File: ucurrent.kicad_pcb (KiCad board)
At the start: 2 copper layers, 44 x 64 mm, 40 parts, among them J1 Conn_01x02, J2 IN_P, J3 IN_N, J4 POWER, J5 Select, J6 OUT_P, J7 OUT_N, SW1 BAT_TEST, SW2 BAT_TEST, U1 TPS3839DBZ, U2 LMV321, U3 MAX4239AUT, U4 MAX4239AUT

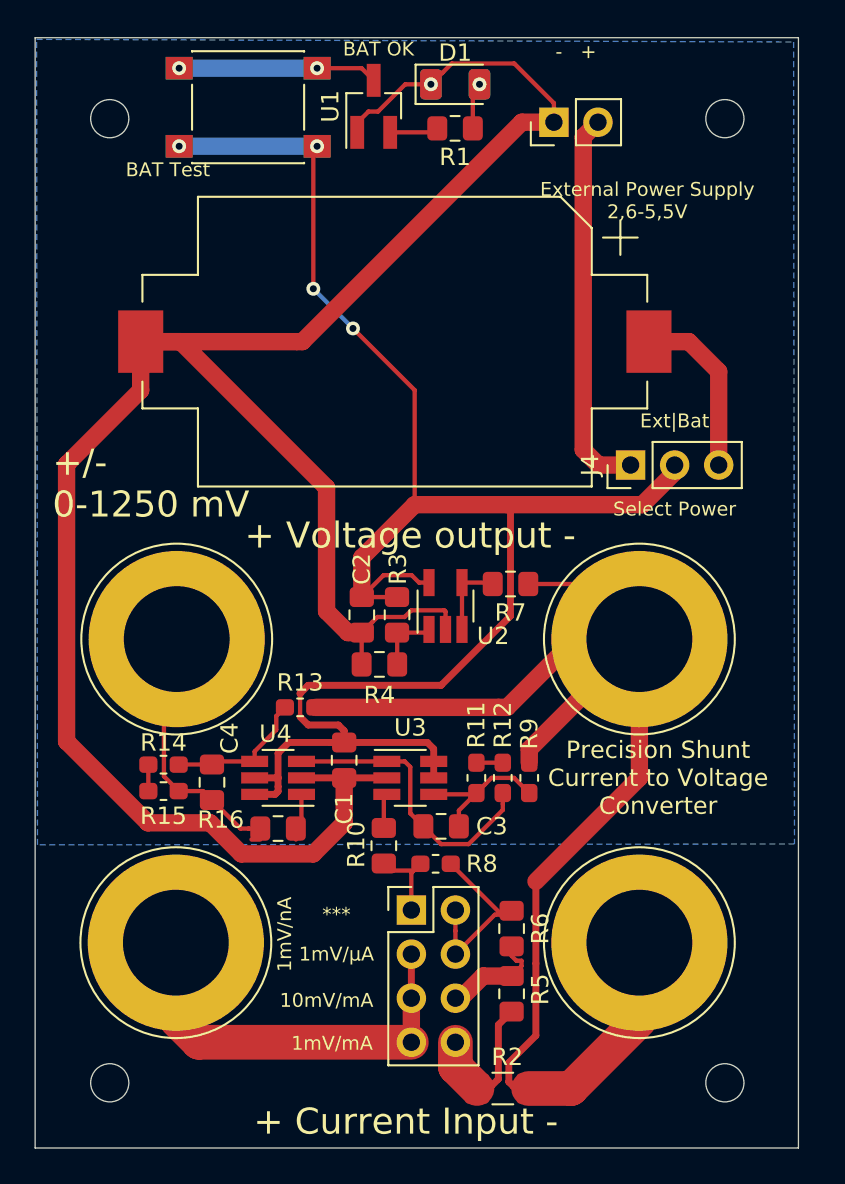
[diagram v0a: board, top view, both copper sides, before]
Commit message: Redid the schematic for voltage measurement, added JLCPCB component references.
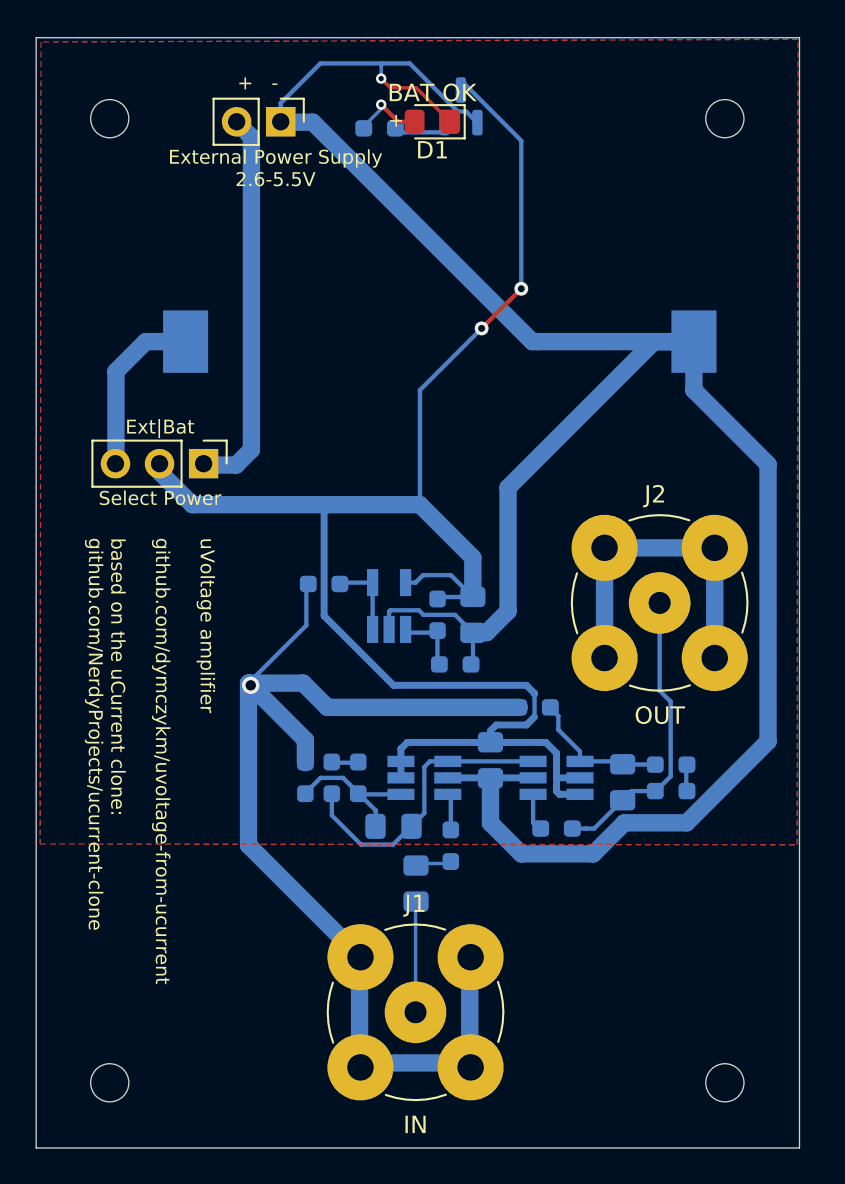
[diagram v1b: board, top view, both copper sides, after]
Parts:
- removed D2: GREEN, LED_SMD:LED_1206_3216Metric
- removed the J3 at (116.3, 93.1)
- removed J5: Select, Connector_PinHeader_2.54mm:PinHeader_2x04_P2.54mm_Vertical
- removed J6: OUT_P, Connector:Banana_Jack_1Pin
- removed J7: OUT_N, Connector:Banana_Jack_1Pin
- removed the R2 at (108.5, 101.5)
- removed the R5 at (109.0, 96.0)
- removed the R6 at (109.0, 92.3)
- removed the R8 at (104.6, 88.5)
- removed SW1, SW2: BAT_TEST, Button_Switch_SMD:SW_Push_1P1T_NO_6x6mm_H9.5mm
- added C1: 100n, Capacitor_SMD:C_0805_2012Metric_Pad1.18x1.45mm_HandSolder, B.Cu at (103.5, 89.7)
- added J1: IN, Connector_Coaxial:BNC_TEConnectivity_1478204_Vertical, F.Cu at (103.4, 97.1)
- BT1, H1, H2, H3, H4, U2, U3, U4: moved to B.Cu
- C2: renamed from C1; footprint Capacitor_SMD:C_0805_2012Metric_Pad1.15x1.40mm_HandSolder -> Capacitor_SMD:C_0805_2012Metric_Pad1.18x1.45mm_HandSolder; moved to B.Cu
- C3: renamed from C2; footprint Capacitor_SMD:C_0805_2012Metric_Pad1.15x1.40mm_HandSolder -> Capacitor_SMD:C_0805_2012Metric_Pad1.18x1.45mm_HandSolder; moved to B.Cu
- C4: renamed from C3; footprint Capacitor_SMD:C_0805_2012Metric_Pad1.15x1.40mm_HandSolder -> Capacitor_SMD:C_0805_2012Metric_Pad1.18x1.45mm_HandSolder; moved to B.Cu
- C5: renamed from C4; footprint Capacitor_SMD:C_0805_2012Metric_Pad1.15x1.40mm_HandSolder -> Capacitor_SMD:C_0805_2012Metric_Pad1.18x1.45mm_HandSolder; moved to B.Cu
- D1: footprint LED_SMD:LED_1206_3216Metric -> LED_SMD:LED_0805_2012Metric_Pad1.15x1.40mm_HandSolder
- J2: value IN_P -> OUT; footprint Connector:Banana_Jack_1Pin -> Connector_Coaxial:BNC_TEConnectivity_1478204_Vertical
- R1: footprint Resistor_SMD:R_0805_2012Metric_Pad1.15x1.40mm_HandSolder -> Resistor_SMD:R_0603_1608Metric_Pad0.98x0.95mm_HandSolder; moved to B.Cu
- R10: renamed from R14; footprint Resistor_SMD:R_0603_1608Metric_Pad1.05x0.95mm_HandSolder -> Resistor_SMD:R_0603_1608Metric_Pad0.98x0.95mm_HandSolder; moved to B.Cu
- R11: renamed from R15; footprint Resistor_SMD:R_0603_1608Metric_Pad1.05x0.95mm_HandSolder -> Resistor_SMD:R_0603_1608Metric_Pad0.98x0.95mm_HandSolder; moved to B.Cu
- R12: renamed from R16; footprint Resistor_SMD:R_0805_2012Metric_Pad1.15x1.40mm_HandSolder -> Resistor_SMD:R_0603_1608Metric_Pad0.98x0.95mm_HandSolder; moved to B.Cu
- R2: renamed from R3; footprint Resistor_SMD:R_0805_2012Metric_Pad1.15x1.40mm_HandSolder -> Resistor_SMD:R_0603_1608Metric_Pad0.98x0.95mm_HandSolder; moved to B.Cu
- R3: renamed from R4; footprint Resistor_SMD:R_0805_2012Metric_Pad1.15x1.40mm_HandSolder -> Resistor_SMD:R_0603_1608Metric_Pad0.98x0.95mm_HandSolder; moved to B.Cu
- R4: renamed from R7; footprint Resistor_SMD:R_0805_2012Metric_Pad1.15x1.40mm_HandSolder -> Resistor_SMD:R_0603_1608Metric_Pad0.98x0.95mm_HandSolder; moved to B.Cu
- R5: renamed from R9; footprint Resistor_SMD:R_0603_1608Metric_Pad1.05x0.95mm_HandSolder -> Resistor_SMD:R_0603_1608Metric_Pad0.98x0.95mm_HandSolder; moved to B.Cu
- R6: renamed from R10; footprint Resistor_SMD:R_0805_2012Metric_Pad1.15x1.40mm_HandSolder -> Resistor_SMD:R_0603_1608Metric_Pad0.98x0.95mm_HandSolder; moved to B.Cu
- R7: renamed from R11; footprint Resistor_SMD:R_0603_1608Metric_Pad1.05x0.95mm_HandSolder -> Resistor_SMD:R_0603_1608Metric_Pad0.98x0.95mm_HandSolder; moved to B.Cu
- R8: renamed from R12; footprint Resistor_SMD:R_0603_1608Metric_Pad1.05x0.95mm_HandSolder -> Resistor_SMD:R_0603_1608Metric_Pad0.98x0.95mm_HandSolder; moved to B.Cu
- R9: renamed from R13; footprint Resistor_SMD:R_0603_1608Metric_Pad1.05x0.95mm_HandSolder -> Resistor_SMD:R_0603_1608Metric_Pad0.98x0.95mm_HandSolder; moved to B.Cu
- U1: footprint Package_TO_SOT_SMD:SOT-23_Handsoldering -> Package_TO_SOT_SMD:SOT-23; moved to B.Cu
- moved H1 35.5 mm to (85.8, 45.6), turned to 180 degrees
- moved H2 35.5 mm to (121.3, 45.6), turned to 180 degrees
- moved H3 35.5 mm to (85.8, 101.1), turned to 180 degrees
- moved H4 35.5 mm to (121.3, 101.1), turned to 180 degrees
- moved J2 34.1 mm to (117.5, 73.5)
- moved R10 29.3 mm to (118.2, 82.8), turned to 180 degrees
- moved R11 29.3 mm to (118.2, 84.3), turned to 0 degrees
- moved J4 24.6 mm to (91.2, 65.5), turned to -90 degrees
- moved C5 23.7 mm to (115.4, 83.8)
- moved R12 16.1 mm to (111.6, 86.5), turned to 180 degrees
- moved U4 16.1 mm to (111.6, 83.6), turned to 0 degrees
- moved J3 15.7 mm to (95.7, 45.7), turned to -90 degrees
- moved R9 13.5 mm to (110.3, 79.5), turned to 180 degrees
- moved R5 12.9 mm to (97.1, 83.6)
- moved R4 10.7 mm to (98.2, 72.4), turned to 0 degrees
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- renumbered J1 to J3
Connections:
- C5 pad 1: Net-(C4-Pad1) (its old number) -> Net-(C5-Pad1)
- J2 pad 1: Net-(J2-Pad1) -> Net-(C5-Pad1)
- R11 pad 1: Net-(C4-Pad1) (its old number) -> Net-(C5-Pad1)
- R12 pad 1: Net-(C4-Pad1) (its old number) -> Net-(C5-Pad1)
- U1 pad 3: Net-(SW1-Pad1) -> +VDC
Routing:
- net Net-(J2-Pad1): track 20.7 -> 0.00 mm
- net Net-(C5-Pad1): track 0.00 -> 17.1 mm
- net Net-(C4-Pad1) (its old number): track 15.5 -> 0.00 mm
- net Net-(SW1-Pad1): track 11.5 -> 0.00 mm, vias 2 -> 0
- net Net-(J5-Pad2): track 11.4 -> 0.00 mm
- net Net-(J5-Pad8): track 8.79 -> 0.00 mm
- net Net-(C1-Pad1): track 0.00 -> 6.39 mm
- net Net-(J5-Pad6): track 6.20 -> 0.00 mm
- net -VDC: track 128.2 -> 133.6 mm
- net Net-(C1-Pad2): track 5.71 -> 2.06 mm
- net +VDC: track 101.9 -> 99.1 mm, vias 4 -> 2
- net GNDREF: track 84.0 -> 85.8 mm, vias 0 -> 1
- net Net-(D1-Pad2): track 2.70 -> 4.18 mm
- added copper zone on F.Cu, net GNDREF
- removed copper zone on B.Cu, net GNDREF
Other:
- net class Default removed
- board text added: "+"
- board text added: "External Power Supply 2.6-5.5V"
- board text added: "uVoltage amplifier github.com/dymczykm/uvoltage-from-ucurrent based on the uCurrent clone: github.com/NerdyProjects/ucurrent-clone"
- board text removed: "***"
- board text removed: "***: suggested second jumper here for increased accuracy for lowest 2 settings"
- board text removed: "+ Current Input -"
- board text removed: "+ Voltage output -"
- board text removed: "+/- 0-1250 mV"
- board text removed: "- Current Input +"
- board text removed: "- Voltage output +"
- board text removed: "10mV/mA"
- board text removed: "1mV/mA"
- board text removed: "1mV/nA"
- board text removed: "1mV/µA"
- board text removed: "2019-11-06"
- board text removed: "BAT Test"
- board text removed: "Bat|Ext"
- board text removed: "External Power Supply 2,6-5,5V"
- board text removed: "Precision Shunt Current to Voltage Converter"
- board text removed: "heavily inspired from µCurrent gold (see eevblog.com). This device does not provide same accuracy or comfort of use as the original. Use of cheaper sense and opamp resistors should lead to +/-1% accuracy on all ranges. Temperature drift should be < 50 ppm, offset voltage and bandwidth unaffected from original (< 50µV, > 300 kHz)"
- board text removed: "https://github.com/NerdyProjects/ucurrent-clone"

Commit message: Updated to LMP7717, v1.1.
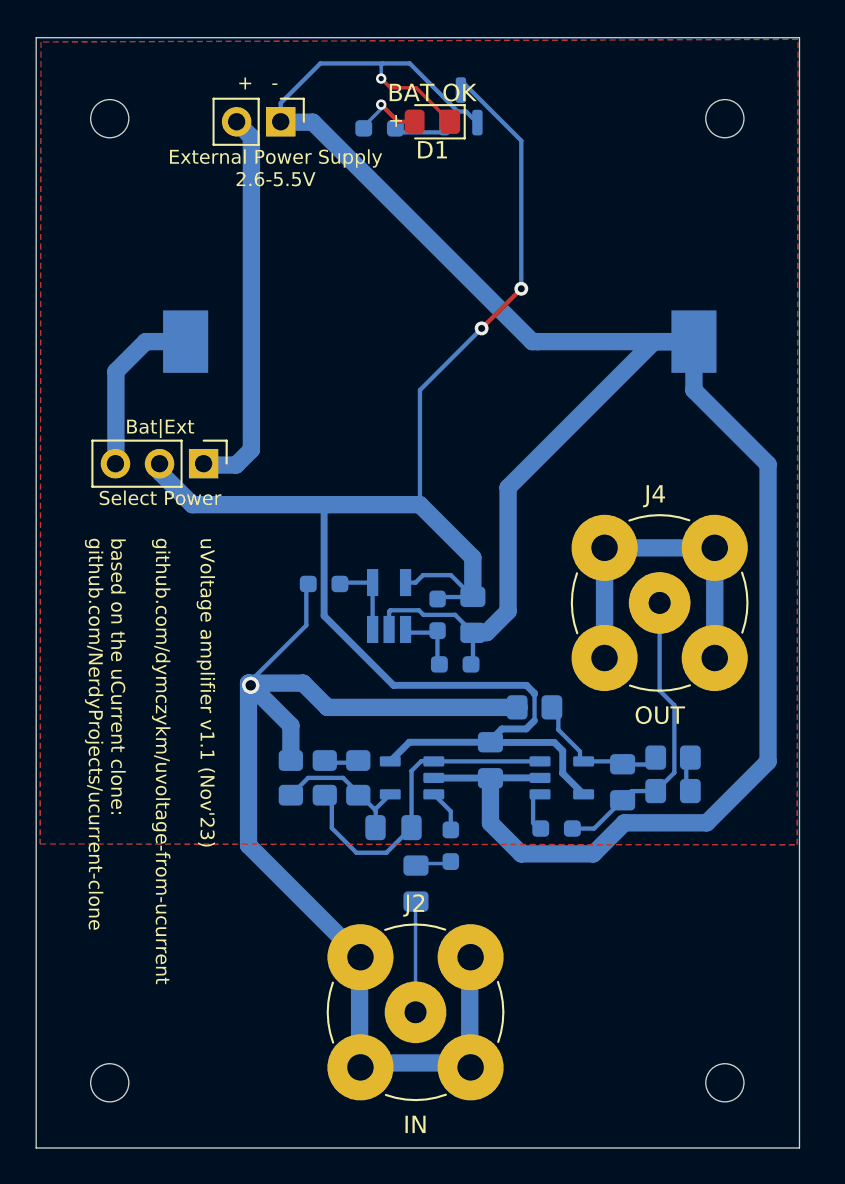
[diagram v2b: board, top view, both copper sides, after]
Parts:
- R10, R11, R5, R7, R8, R9: footprint Resistor_SMD:R_0603_1608Metric_Pad0.98x0.95mm_HandSolder -> Resistor_SMD:R_0805_2012Metric_Pad1.20x1.40mm_HandSolder
- U1: value TPS3839DBZ -> TPS3839K33DBZ
- U3, U4: value MAX4239AUT -> LMP7717MF; footprint Package_TO_SOT_SMD:SOT-23-6_Handsoldering -> marcin_library:SOT95P280X145-5N
- moved R5 0.84 mm to (96.2, 83.6)
- moved U3 0.71 mm to (103.2, 83.6)
- moved R10 0.42 mm to (118.3, 82.4)
- moved R8 0.41 mm to (98.2, 83.6)
- moved U4 0.30 mm to (111.9, 83.6)
- moved R11 0.11 mm to (118.3, 84.3)
- moved C4 0.08 mm to (102.2, 86.4)
- renumbered J3 to J1, J1 to J2, J4 to J3, J2 to J4
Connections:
- net Net-(BT1-Pad1) renamed /BAT_POS
- net Net-(J3-Pad2) renamed /EXT_POS
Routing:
- net +VDC: track 99.1 -> 96.5 mm
- net Net-(C4-Pad1): track 17.1 -> 18.6 mm
- net -VDC: track 133.6 -> 135.1 mm
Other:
- board text added: "Bat|Ext"
- board text added: "uVoltage amplifier v1.1 (Nov'23) github.com/dymczykm/uvoltage-from-ucurrent based on the uCurrent clone: github.com/NerdyProjects/ucurrent-clone"
- board text removed: "Ext|Bat"
- board text removed: "uVoltage amplifier github.com/dymczykm/uvoltage-from-ucurrent based on the uCurrent clone: github.com/NerdyProjects/ucurrent-clone"
